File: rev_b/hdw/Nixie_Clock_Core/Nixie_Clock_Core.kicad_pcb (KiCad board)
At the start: 6 copper layers, 200 x 50 mm, 330 parts, among them J1301 USB_B_Mini, J1901 Conn_02x32_Top_Bottom, J201 +24V IN, J2101 I2C, J2102 USB UART, J801 PICKIT4, Q2101 BSS214NW, Q401 BSS214NW, Q402 ZXMS6004FFTA, Q601 IRFL214, Q701 BSS192PH6327FTSA1, Q801 BSS214NW, SW801 MRST, U1001 PIC32MZ2048EFG100_IPF, U1101 74LVC1G97, U1201 DS3231MZ, U1202 TLV6700, U1301 TLV6700, U1302 FT234XD, U1303 74LVC1G97, U1304 ISO7321C, U1305 TPD3S014DBVR, U1401 DS1683, U1501 74LVC1G97, U1502 74LVC1G97, U1503 74LVC1G97, U1504 74LVC1G97, U1505 74LVC1G97, U1601 74LVC1G97, U1602 74LVC1G97, U1603 74LVC1G97, U1604 74LVC1G97, U1701 74VHC541, U1702 74VHC541, U1703 74VHC541, U1801 TCA9803, U1802 74VHC541, U201 TPS26600RHFT, U2101 LTC6900, U2102 74LVC1G97, U2103 MCP9804, U301 INA219BxDCN, U302 MCP9804, U401 LT8609A-DD, U501 INA219BxDCN, U502 MCP9804, U601 TLV6700, U602 LT3757, U603 TLV6700, U701 OPA333xxDCK, U702 MCP9804, U703 INA219BxDCN, U704 OPA333xxDCK, U705 OPA333xxDCK, X1101 ASE-8.000MHz, X1102 ECS-327KE

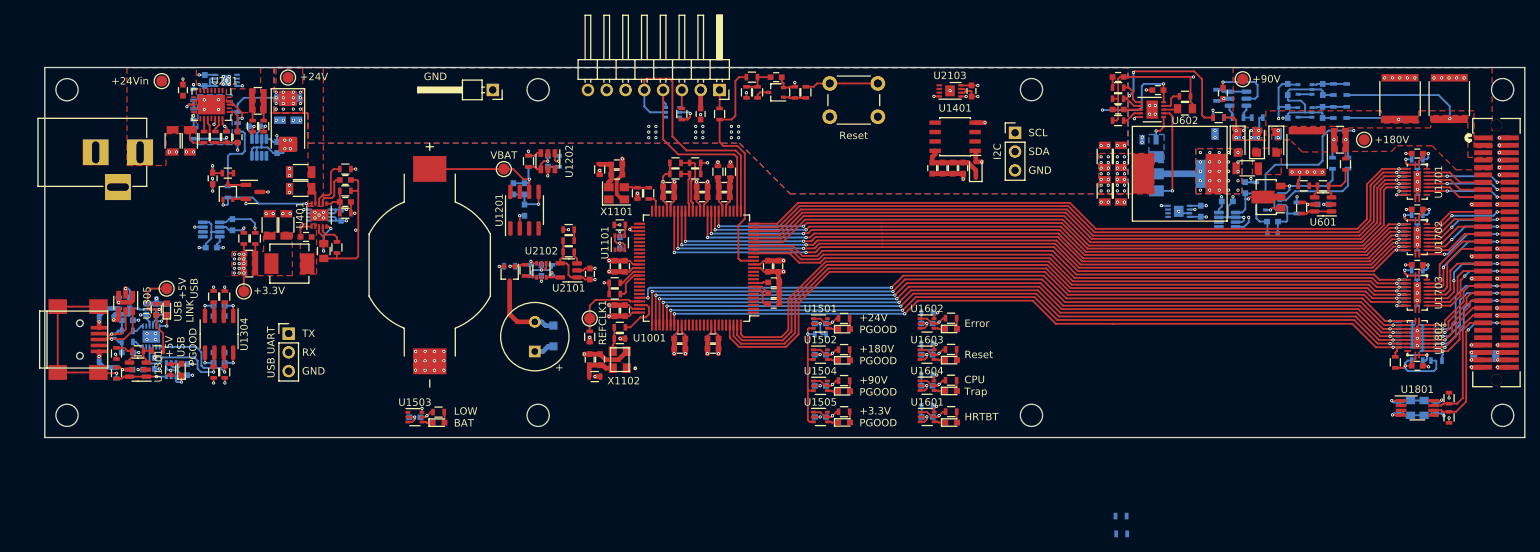
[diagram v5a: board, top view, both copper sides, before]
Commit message: lots more core board routing
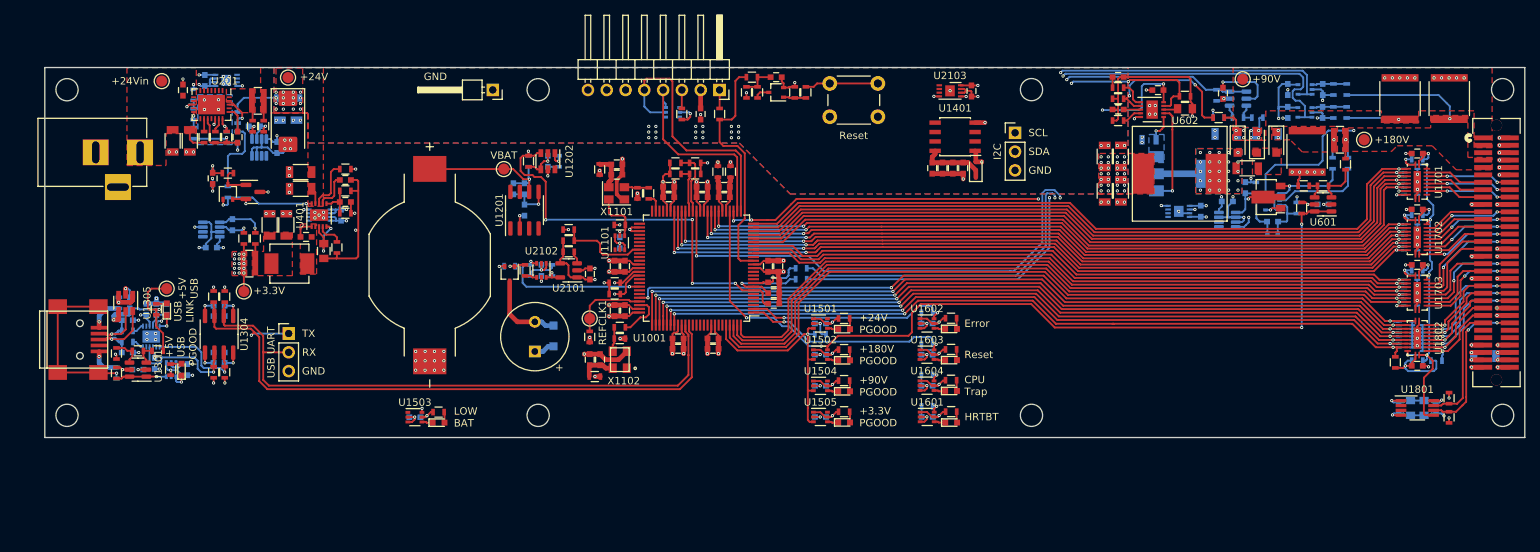
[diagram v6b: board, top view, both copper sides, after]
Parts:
- moved R708 56.2 mm to (137.2, 95.9)
- moved R707 53.8 mm to (137.2, 97.4)
- moved C906 0.23 mm to (120.6, 105.4)
- moved C908 0.23 mm to (120.6, 106.8)
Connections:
- U1001 pad 1: unconnected-(U1001-RG15/AN23/AERXERR-Pad1) -> Reset_LED
- U1001 pad 10: POS180_RUN -> unconnected-(U1001-RG6/AN14/C1IND/ECOL/RPG6/SCK2-Pad10)
- U1001 pad 11: POS180_PGOOD -> unconnected-(U1001-RG7/EBIA4/AN13/C1INC/ECRS/RPG7/SDA4/PMA4-Pad11)
- U1001 pad 12: POS90_PGOOD -> unconnected-(U1001-RG8/EBIA3/AN12/C2IND/ERXDV/ECRSDV/AERXDV/AECRSDV/RPG8/SCL4/PMA3-Pad12)
- U1001 pad 16: VBAT_PGOOD -> unconnected-(U1001-RG9/EBIA2/AN11/C2INC/ERXCLK/EREFCLK/AERXCLK/AEREFCLK/RPG9/PMA2-Pad16)
- U1001 pad 2: unconnected-(U1001-RA5/EBIA5/AN34/PMA5-Pad2) -> Error_LED
- U1001 pad 28: unconnected-(U1001-RA9/VREF-/CVREF-/AN27/AERXD2-Pad28) -> POS180_RUN
- U1001 pad 29: unconnected-(U1001-RA10/VREF+/CVREF+/AN28/AERXD3-Pad29) -> POS180_PGOOD
- U1001 pad 38: unconnected-(U1001-RA1/TCK/EBIA19/AN29-Pad38) -> POS90_PGOOD
- U1001 pad 4: Reset_LED -> unconnected-(U1001-RE6/EBID6/AN16/PMD6-Pad4)
- U1001 pad 5: Error_LED -> unconnected-(U1001-RE7/EBID7/AN15/PMD7-Pad5)
- U1001 pad 68: unconnected-(U1001-RD9/EBIA15/RPD9/PMCS2/PMA15-Pad68) -> Buzzer_Enable
- U1001 pad 89: unconnected-(U1001-RA6/TRCLK/SQICLK-Pad89) -> VBAT_PGOOD
- U1001 pad 91: unconnected-(U1001-RE0/EBID0/PMD0-Pad91) -> Heartbeat_LED
- U1001 pad 94: unconnected-(U1001-RE1/EBID1/PMD1-Pad94) -> CPU_Trap_LED
- U1001 pad 96: unconnected-(U1001-RG12/TRD1/SQID1-Pad96) -> PGOOD_LED_SHDN
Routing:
- net POS180_PGOOD: track 4.16 -> 117.2 mm, vias 0 -> 4
- net POS90_PGOOD: track 4.14 -> 106.7 mm, vias 0 -> 3
- net Net-(U705--): track 1.90 -> 102.2 mm, vias 0 -> 2
- net Net-(U704--): track 1.90 -> 97.0 mm, vias 0 -> 2
- net USB_UART_TX: track 1.91 -> 88.5 mm, vias 0 -> 1
- net USB_UART_RX: track 1.92 -> 83.7 mm
- net POS180_RUN: track 3.17 -> 83.6 mm, vias 0 -> 5
- net VBAT_ADC: track 6.48 -> 55.7 mm, vias 1 -> 5
- net ~{IO_Level_Shift_Enable}: track 26.1 -> 63.8 mm
- net Reset_LED: track 1.38 -> 28.2 mm, vias 1 -> 2
- net Error_LED: track 1.67 -> 27.8 mm, vias 1 -> 2
- net Buzzer_Enable: track 1.35 -> 20.7 mm, vias 1 -> 2
- net PGOOD_LED_SHDN: track 16.9 -> 31.4 mm
- net Telemetry_Hardstrap: track 1.50 -> 12.0 mm
- net GND: track 323.4 -> 313.8 mm, vias 176 -> 179
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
